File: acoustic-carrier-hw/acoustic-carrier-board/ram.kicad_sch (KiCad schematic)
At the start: 15 parts, among them IC1 ECP5-BGA256, IC2 MT41K256M16TW-107_P

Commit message: [carrier] Added separate buses for ddr3 ctrl-cmd and dq-groups
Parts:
- removed C40, C46: 0.1uF, Capacitor_SMD:C_0402_1005Metric, symbol Device:C_Small
- removed C47: 1uF, Capacitor_SMD:C_0805_2012Metric, symbol Device:C_Small
- removed C70: 22uF, Capacitor_SMD:C_0603_1608Metric, symbol Device:C_Small
- removed IC2: MT41K256M16TW-107_P, fpga:BGA96C80P9X16_800X1400X120, symbol MT41K256M16TW-107-P:MT41K256M16TW-107_P
- added C120, C58, C59: 10nF, Capacitor_SMD:C_0402_1005Metric, symbol Device:C_Small
- added C121, C122, C124, C125, C126, C49, C57: 0.1uF, Capacitor_SMD:C_0402_1005Metric, symbol Device:C_Small
- added C123, C127: 22uF, Capacitor_SMD:C_0603_1608Metric, symbol Device:C_Small
- added C5, C6: 10uF, Capacitor_SMD:C_0603_1608Metric, symbol Device:C_Small
- added IC3: MT41K256M16TW-107_P, fpga:BGA96C80P9X16_800X1400X120, symbol MT41K256M16TW-107-P:MT41K256M16TW-107_P
- added L10, L11, L9: 120@100MHz, Inductor_SMD:L_0603_1608Metric, symbol Device:L_Small
- C34, C35: value 22uF -> 10nF; footprint Capacitor_SMD:C_0603_1608Metric -> Capacitor_SMD:C_0402_1005Metric; LPN C59461 -> CL05B103KB5NNNC; MPN CL10A226MQ8NRNC -> C15195
- C37, C42: value 0.1uF -> 10nF; LPN C307331 -> CL05B103KB5NNNC; MPN CL05B104KB54PNC -> C15195
- C43: value 10nF -> 0.1uF; LPN CL05B103KB5NNNC -> C307331; MPN C15195 -> CL05B104KB54PNC
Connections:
- net GND: now also C120.2, C121.2, C122.2, C123.2, C124.2, C125.2, C126.2, C127.2, C49.2, C5.2, C57.2, C58.2, C59.2, C6.2, IC3.A9 (VSS_1), IC3.B1 (VSSQ_1), IC3.B3 (VSS_2), IC3.B9 (VSSQ_2), IC3.D1 (VSSQ_3), IC3.D8 (VSSQ_4), IC3.E1 (VSS_3), IC3.E2 (VSSQ_5), IC3.E8 (VSSQ_6), IC3.F9 (VSSQ_7), IC3.G1 (VSSQ_8), IC3.G8 (VSS_4), IC3.G9 (VSSQ_9), IC3.J2 (VSS_5), IC3.J8 (VSS_6), IC3.M1 (VSS_7), IC3.M9 (VSS_8), IC3.P1 (VSS_9), IC3.P9 (VSS_10), IC3.T1 (VSS_11), IC3.T9 (VSS_12)
- net VDDR3L_0.675: no longer IC1.G14 (PR14C/VREF1_2)
- net VDDR3L_1.35: now also L10.2, L11.2, L9.2; no longer C34.1, C35.1, C37.1, C42.1, IC1.H11 (VCCIO2_1), IC1.J11 (VCCIO2_2), IC1.J6 (VCCIO6_1), IC1.J7 (VCCIO6_2)
- net VDRR3L_0.675: now also IC1.G14 (PR14C/VREF1_2), C120.1, C121.1, IC3.H1 (VREFDQ), IC3.M8 (VREFCA); no longer C39.1, C43.1
- net LPDDR3.LDM: now reaches IC1.F13 (PR8C)
- net LPDDR3.LDM: now also IC3.E7 (LDM)
- net LPDDR3.DQ14: now reaches IC1.J15 (PR23B/PCLKC2_1)
- net LPDDR3.DQ14: now also IC3.B8 (DQ14)
- net LPDDR3.DQ13: now reaches IC1.J16 (PR23A/PCLKT2_1)
- net LPDDR3.DQ13: now also IC3.A2 (DQ13)
- net LPDDR3.DQ12: now reaches IC1.K14 (PR20D/GR_PCLK2_0)
- net LPDDR3.DQ12: now also IC3.A7 (DQ12)
- net LPDDR3.UDM: now reaches IC1.K15 (PR23D/PCLKC2_0/RDQ20)
- net LPDDR3.UDM: now also IC3.D3 (UDM)
- net LPDDR3.DQ15: now reaches IC1.K16 (PR23C/PCLKT2_0)
- net LPDDR3.DQ15: now also IC3.A3 (DQ15)
- net LPDDR3.A14: now reaches IC1.L1 (PL26A/LDQ32/PCLKT6_1)
- net LPDDR3.A14: now also IC3.T7 (A14)
- net at R54.1: now also IC3.L8 (ZQ)
- net RAM_A0 renamed LPDDR3.A0
- net LPDDR3.A0: now also IC3.N3 (A0)
- net RAM_A1 renamed LPDDR3.A1
- net LPDDR3.A1: now also IC3.P7 (A1)
- net RAM_A10 renamed LPDDR3.A9
- net LPDDR3.A9: now also IC3.R3 (A9)
- net RAM_A11 renamed LPDDR3.A10
- net LPDDR3.A10: now also IC3.L7 (A10/AP)
- net RAM_A12 renamed LPDDR3.A11
- net LPDDR3.A11: now also IC3.R7 (A11)
- net RAM_A13 renamed LPDDR3.A12
- net LPDDR3.A12: now also IC3.N7 (A12/BC#)
- net RAM_A14 renamed LPDDR3.A13
- net LPDDR3.A13: now also IC3.T3 (A13)
- net RAM_A2: no longer names the net of IC1.M4 (PL35C)
- net RAM_A3 renamed LPDDR3.A2
- net LPDDR3.A2: now also IC3.P3 (A2)
- net RAM_A4 renamed LPDDR3.A3
- net LPDDR3.A3: now also IC3.N2 (A3)
- net RAM_A5 renamed LPDDR3.A4
- net LPDDR3.A4: now also IC3.P8 (A4)
- net RAM_A6 renamed LPDDR3.A5
- net LPDDR3.A5: now also IC3.P2 (A5)
- net RAM_A7 renamed LPDDR3.A6
- net LPDDR3.A6: now also IC3.R8 (A6)
- net RAM_A8 renamed LPDDR3.A7
- net LPDDR3.A7: now also IC3.R2 (A7)
- net RAM_A9 renamed LPDDR3.A8
- net LPDDR3.A8: now also IC3.T8 (A8)
- net RAM_BA0 renamed LPDDR3.ODT
- net LPDDR3.ODT: now also IC3.K1 (ODT)
- net RAM_BA1: no longer names the net of IC1.T2 (PL38D)
- net RAM_BA2: no longer names the net of IC1.R2 (PL38C)
- net RAM_CAS# renamed LPDDR3.BA2
- net LPDDR3.BA2: now also IC3.M3 (BA2)
- net RAM_CK+ renamed LPDDR3.CK#
- net LPDDR3.CK#: now also IC3.K7 (CK#)
- net RAM_CK- renamed LPDDR3.CK
- net LPDDR3.CK: now also IC3.J7 (CK)
- net RAM_CKE renamed LPDDR3.RAS#
- net LPDDR3.RAS#: now also IC3.J3 (RAS#)
- net RAM_CS# renamed LPDDR3.CKE
- net LPDDR3.CKE: now also IC3.K9 (CKE)
- net RAM_D0 renamed LPDDR3.DQ0
- net LPDDR3.DQ0: now also IC3.E3 (DQ0)
- net RAM_D1 renamed LPDDR3.DQ1
- net LPDDR3.DQ1: now also IC3.F7 (DQ1)
- net RAM_D10: no longer names the net of IC1.H14 (PR14D)
- net RAM_D11: no longer names the net of IC1.H12 (PR17A)
- net RAM_D12 renamed LPDDR3.DQ8
- net LPDDR3.DQ8: now also IC3.D7 (DQ8)
- net RAM_D13 renamed LPDDR3.DQ9
- net LPDDR3.DQ9: now also IC3.C3 (DQ9)
- net RAM_D14 renamed LPDDR3.DQ10
- net LPDDR3.DQ10: now also IC3.C8 (DQ10)
- net RAM_D15 renamed LPDDR3.DQ11
- net LPDDR3.DQ11: now also IC3.C2 (DQ11)
- net RAM_D2 renamed LPDDR3.DQ2
- net LPDDR3.DQ2: now also IC3.F2 (DQ2)
- net RAM_D3 renamed LPDDR3.DQ3
- net LPDDR3.DQ3: now also IC3.F8 (DQ3)
- net RAM_D4 renamed LPDDR3.DQ4
- net LPDDR3.DQ4: now also IC3.H3 (DQ4)
- net RAM_D5 renamed LPDDR3.DQ5
- net LPDDR3.DQ5: now also IC3.H8 (DQ5)
- net RAM_D6 renamed LPDDR3.DQ6
- net LPDDR3.DQ6: now also IC3.G2 (DQ6)
- net RAM_D7 renamed LPDDR3.DQ7
- net LPDDR3.DQ7: now also IC3.H7 (DQ7)
- net RAM_D8: no longer names the net of IC1.F16 (PR14A/RDQ20)
- net RAM_D9: no longer names the net of IC1.G15 (PR14B)
- net RAM_LDM renamed LPDDR3.CAS#
- net LPDDR3.CAS#: now also IC3.K3 (CAS#)
- net RAM_LDQS+ renamed LPDDR3.LDQS
- net LPDDR3.LDQS: now also IC3.F3 (LDQS)
- net RAM_LDQS- renamed LPDDR3.LDQS#
- net LPDDR3.LDQS#: now also IC3.G3 (LDQS#)
- net RAM_ODT renamed LPDDR3.BA0
- net LPDDR3.BA0: now also IC3.M2 (BA0)
- net RAM_RAS# renamed LPDDR3.BA1
- net LPDDR3.BA1: now also IC3.N8 (BA1)
- net RAM_RESET# renamed LPDDR3.WE#
- net LPDDR3.WE#: now also IC3.L3 (WE#)
- net RAM_UDM renamed LPDDR3.CS#
- net LPDDR3.CS#: now also IC3.L2 (CS#)
- net RAM_UDQS+ renamed LPDDR3.UDQS
- net LPDDR3.UDQS: now also IC3.B7 (UDQS#)
- net RAM_UDQS- renamed LPDDR3.UDQS#
- net LPDDR3.UDQS#: now also IC3.C7 (UDQS)
- net RAM_WE# renamed LPDDR3.RESET#
- net LPDDR3.RESET#: now also IC3.T2 (RESET#)
- new net VDDR_BANK: C49.1, C5.1, C57.1, C58.1, C59.1, C6.1, IC1.H11 (VCCIO2_1), IC1.J11 (VCCIO2_2), IC1.J6 (VCCIO6_1), IC1.J7 (VCCIO6_2), L11.1
- new net VDDR_CORE: C124.1, C125.1, C126.1, C127.1, C37.1, C42.1, IC3.B2 (VDD_1), IC3.D9 (VDD_2), IC3.G7 (VDD_3), IC3.K2 (VDD_4), IC3.K8 (VDD_5), IC3.N1 (VDD_6), IC3.N9 (VDD_7), IC3.R1 (VDD_8), IC3.R9 (VDD_9), L9.1
- new net VDDR_DQ: C122.1, C123.1, C34.1, C35.1, C39.1, C43.1, IC3.A1 (VDDQ_1), IC3.A8 (VDDQ_2), IC3.C1 (VDDQ_3), IC3.C9 (VDDQ_4), IC3.D2 (VDDQ_5), IC3.E9 (VDDQ_6), IC3.F1 (VDDQ_7), IC3.H2 (VDDQ_8), IC3.H9 (VDDQ_9), L10.1
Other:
- note added: "DDR3L DECOUPLING"
- moved on the sheet: C38, C80, IC1D, IC1F, R54

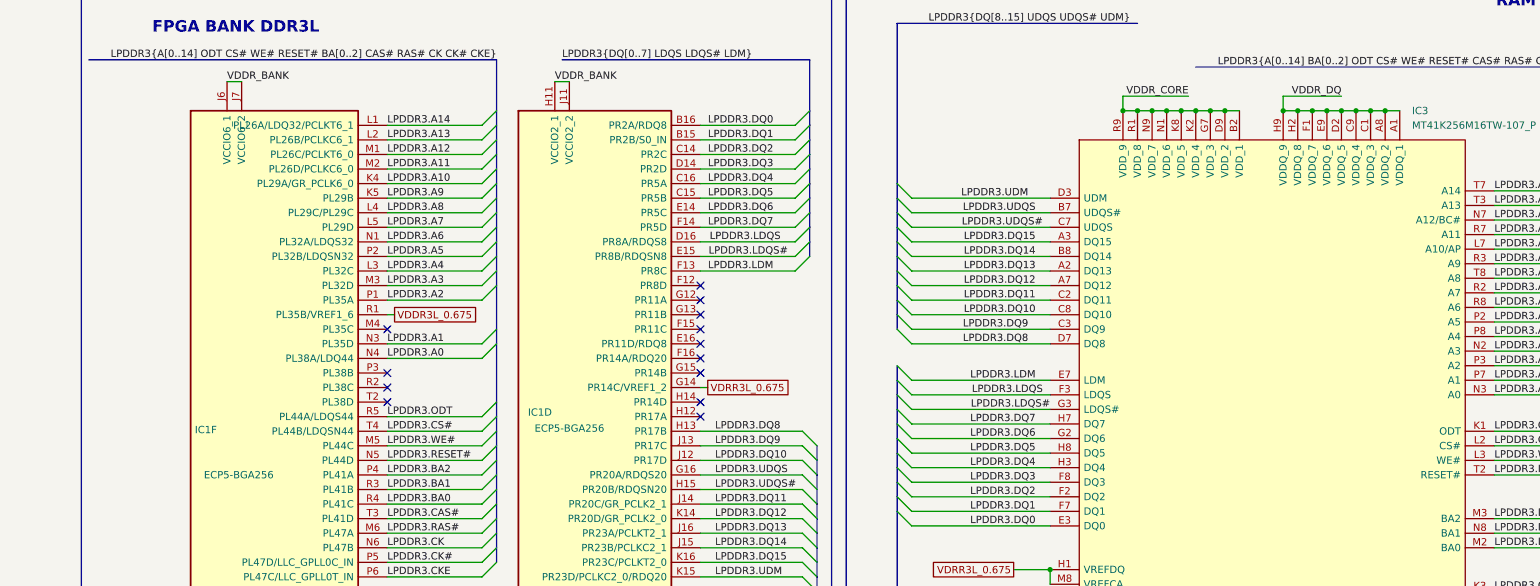
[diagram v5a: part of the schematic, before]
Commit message: [carrier] Fixed error in ethernet power supply, separated footprints + symbols into library (next) check whether supply should be DVDDH
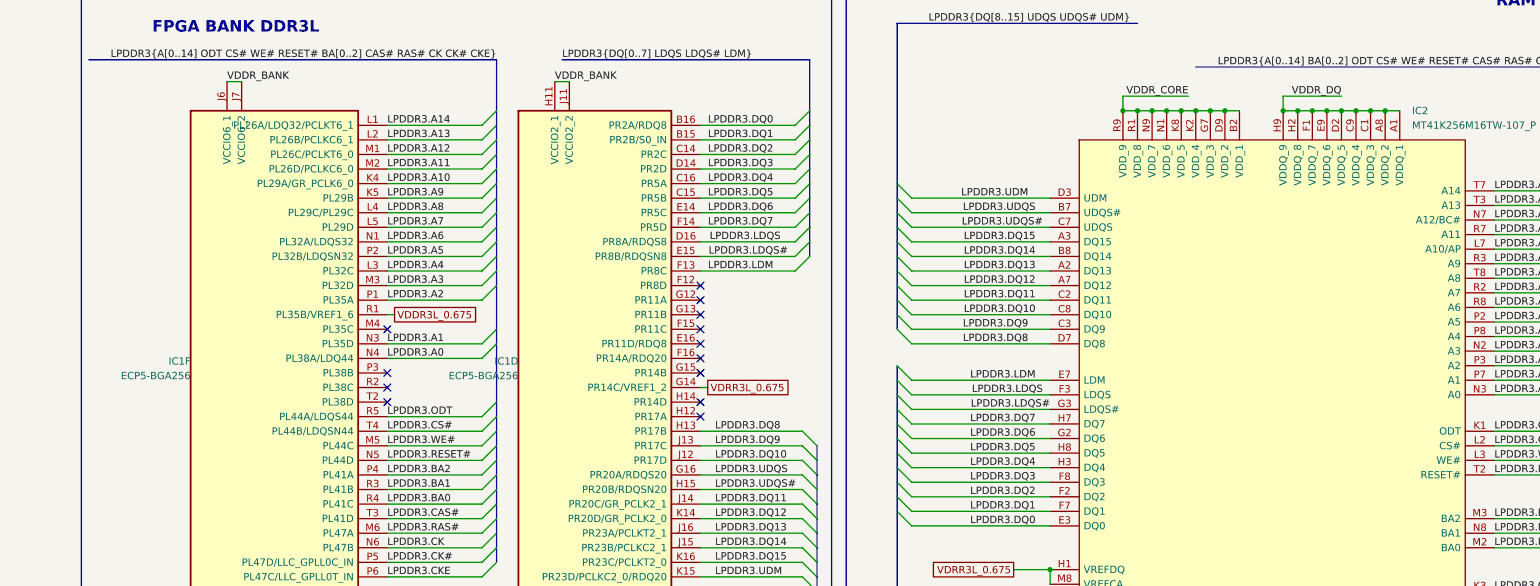
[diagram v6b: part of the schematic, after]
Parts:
- removed IC1: ECP5-BGA256, fpga:BGA256C80P16X16_1400X1400X170, symbol ecp5bga256:ECP5-BGA256
- removed IC3: MT41K256M16TW-107_P, fpga:BGA96C80P9X16_800X1400X120, symbol MT41K256M16TW-107-P:MT41K256M16TW-107_P
- added IC1: ECP5-BGA256, iw-fpga_mcu:BGA256C80P16X16_1400X1400X170, symbol iw-fpga_mcu:ECP5-BGA256
- added IC2: MT41K256M16TW-107_P, iw-memory:BGA96C80P9X16_800X1400X120, symbol iw-memory:MT41K256M16TW-107_P
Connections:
- net GND: now also IC2.A9 (VSS_1), IC2.B1 (VSSQ_1), IC2.B3 (VSS_2), IC2.B9 (VSSQ_2), IC2.D1 (VSSQ_3), IC2.D8 (VSSQ_4), IC2.E1 (VSS_3), IC2.E2 (VSSQ_5), IC2.E8 (VSSQ_6), IC2.F9 (VSSQ_7), IC2.G1 (VSSQ_8), IC2.G8 (VSS_4), IC2.G9 (VSSQ_9), IC2.J2 (VSS_5), IC2.J8 (VSS_6), IC2.M1 (VSS_7), IC2.M9 (VSS_8), IC2.P1 (VSS_9), IC2.P9 (VSS_10), IC2.T1 (VSS_11), IC2.T9 (VSS_12)
- net LPDDR3.A0: now also IC1.N4 (PL38A/LDQ44), IC2.N3 (A0)
- net LPDDR3.A1: now also IC1.N3 (PL35D), IC2.P7 (A1)
- net LPDDR3.A10: now also IC1.K4 (PL29A/GR_PCLK6_0), IC2.L7 (A10/AP)
- net LPDDR3.A11: now also IC1.M2 (PL26D/PCLKC6_0), IC2.R7 (A11)
- net LPDDR3.A12: now also IC1.M1 (PL26C/PCLKT6_0), IC2.N7 (A12/BC#)
- net LPDDR3.A13: now also IC1.L2 (PL26B/PCLKC6_1), IC2.T3 (A13)
- net LPDDR3.A14: now also IC1.L1 (PL26A/LDQ32/PCLKT6_1), IC2.T7 (A14)
- net LPDDR3.A2: now also IC1.P1 (PL35A), IC2.P3 (A2)
- net LPDDR3.A3: now also IC1.M3 (PL32D), IC2.N2 (A3)
- net LPDDR3.A4: now also IC1.L3 (PL32C), IC2.P8 (A4)
- net LPDDR3.A5: now also IC1.P2 (PL32B/LDQSN32), IC2.P2 (A5)
- net LPDDR3.A6: now also IC1.N1 (PL32A/LDQS32), IC2.R8 (A6)
- net LPDDR3.A7: now also IC1.L5 (PL29D), IC2.R2 (A7)
- net LPDDR3.A8: now also IC1.L4 (PL29C/PL29C), IC2.T8 (A8)
- net LPDDR3.A9: now also IC1.K5 (PL29B), IC2.R3 (A9)
- net LPDDR3.BA0: now also IC1.R4 (PL41C), IC2.M2 (BA0)
- net LPDDR3.BA1: now also IC1.R3 (PL41B), IC2.N8 (BA1)
- net LPDDR3.BA2: now also IC1.P4 (PL41A), IC2.M3 (BA2)
- net LPDDR3.CAS#: now also IC1.T3 (PL41D), IC2.K3 (CAS#)
- net LPDDR3.CK: now also IC1.N6 (PL47B), IC2.J7 (CK)
- net LPDDR3.CK#: now also IC1.P5 (PL47D/LLC_GPLL0C_IN), IC2.K7 (CK#)
- net LPDDR3.CKE: now also IC1.P6 (PL47C/LLC_GPLL0T_IN), IC2.K9 (CKE)
- net LPDDR3.CS#: now also IC1.T4 (PL44B/LDQSN44), IC2.L2 (CS#)
- net LPDDR3.DQ0: now also IC1.B16 (PR2A/RDQ8), IC2.E3 (DQ0)
- net LPDDR3.DQ1: now also IC1.B15 (PR2B/S0_IN), IC2.F7 (DQ1)
- net LPDDR3.DQ10: now also IC1.J12 (PR17D), IC2.C8 (DQ10)
- net LPDDR3.DQ11: now also IC1.J14 (PR20C/GR_PCLK2_1), IC2.C2 (DQ11)
- net LPDDR3.DQ12: now also IC1.K14 (PR20D/GR_PCLK2_0), IC2.A7 (DQ12)
- net LPDDR3.DQ13: now also IC1.J16 (PR23A/PCLKT2_1), IC2.A2 (DQ13)
- net LPDDR3.DQ14: now also IC1.J15 (PR23B/PCLKC2_1), IC2.B8 (DQ14)
- net LPDDR3.DQ15: now also IC1.K16 (PR23C/PCLKT2_0), IC2.A3 (DQ15)
- net LPDDR3.DQ2: now also IC1.C14 (PR2C), IC2.F2 (DQ2)
- net LPDDR3.DQ3: now also IC1.D14 (PR2D), IC2.F8 (DQ3)
- net LPDDR3.DQ4: now also IC1.C16 (PR5A), IC2.H3 (DQ4)
- net LPDDR3.DQ5: now also IC1.C15 (PR5B), IC2.H8 (DQ5)
- net LPDDR3.DQ6: now also IC1.E14 (PR5C), IC2.G2 (DQ6)
- net LPDDR3.DQ7: now also IC1.F14 (PR5D), IC2.H7 (DQ7)
- net LPDDR3.DQ8: now also IC1.H13 (PR17B), IC2.D7 (DQ8)
- net LPDDR3.DQ9: now also IC1.J13 (PR17C), IC2.C3 (DQ9)
- net LPDDR3.LDM: now also IC1.F13 (PR8C), IC2.E7 (LDM)
- net LPDDR3.LDQS: now also IC1.D16 (PR8A/RDQS8), IC2.F3 (LDQS)
- net LPDDR3.LDQS#: now also IC1.E15 (PR8B/RDQSN8), IC2.G3 (LDQS#)
- net LPDDR3.ODT: now also IC1.R5 (PL44A/LDQS44), IC2.K1 (ODT)
- net LPDDR3.RAS#: now also IC1.M6 (PL47A), IC2.J3 (RAS#)
- net LPDDR3.RESET#: now also IC1.N5 (PL44D), IC2.T2 (RESET#)
- net LPDDR3.UDM: now also IC1.K15 (PR23D/PCLKC2_0/RDQ20), IC2.D3 (UDM)
- net LPDDR3.UDQS: now also IC1.G16 (PR20A/RDQS20), IC2.B7 (UDQS#)
- net LPDDR3.UDQS#: now also IC1.H15 (PR20B/RDQSN20), IC2.C7 (UDQS)
- net LPDDR3.WE#: now also IC1.M5 (PL44C), IC2.L3 (WE#)
- net VDDR3L_0.675: now also IC1.R1 (PL35B/VREF1_6)
- net VDDR_BANK: now also IC1.H11 (VCCIO2_1), IC1.J11 (VCCIO2_2), IC1.J6 (VCCIO6_1), IC1.J7 (VCCIO6_2)
- net VDDR_CORE: now also IC2.B2 (VDD_1), IC2.D9 (VDD_2), IC2.G7 (VDD_3), IC2.K2 (VDD_4), IC2.K8 (VDD_5), IC2.N1 (VDD_6), IC2.N9 (VDD_7), IC2.R1 (VDD_8), IC2.R9 (VDD_9)
- net VDDR_DQ: now also IC2.A1 (VDDQ_1), IC2.A8 (VDDQ_2), IC2.C1 (VDDQ_3), IC2.C9 (VDDQ_4), IC2.D2 (VDDQ_5), IC2.E9 (VDDQ_6), IC2.F1 (VDDQ_7), IC2.H2 (VDDQ_8), IC2.H9 (VDDQ_9)
- net VDRR3L_0.675: now also IC1.G14 (PR14C/VREF1_2), IC2.H1 (VREFDQ), IC2.M8 (VREFCA)
- net at R54.1: now also IC2.L8 (ZQ)

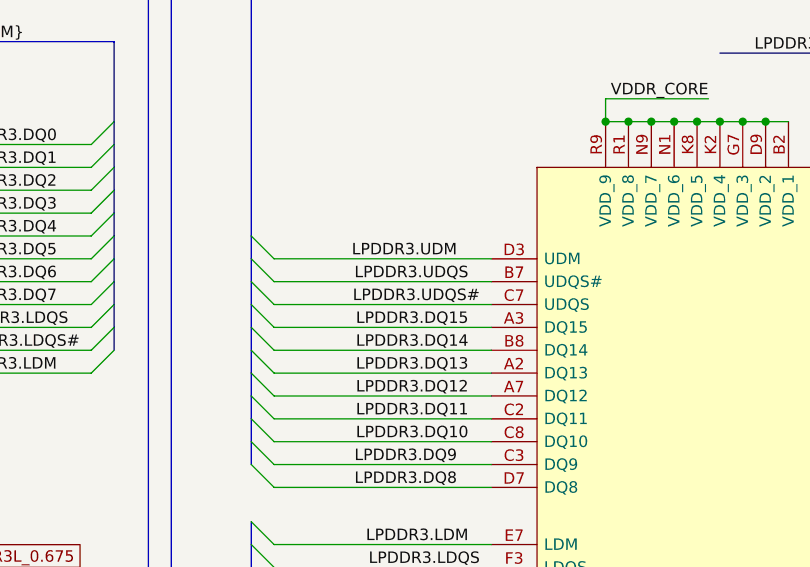
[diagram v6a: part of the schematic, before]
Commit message: [carrier] Signal switch-around in ddr3
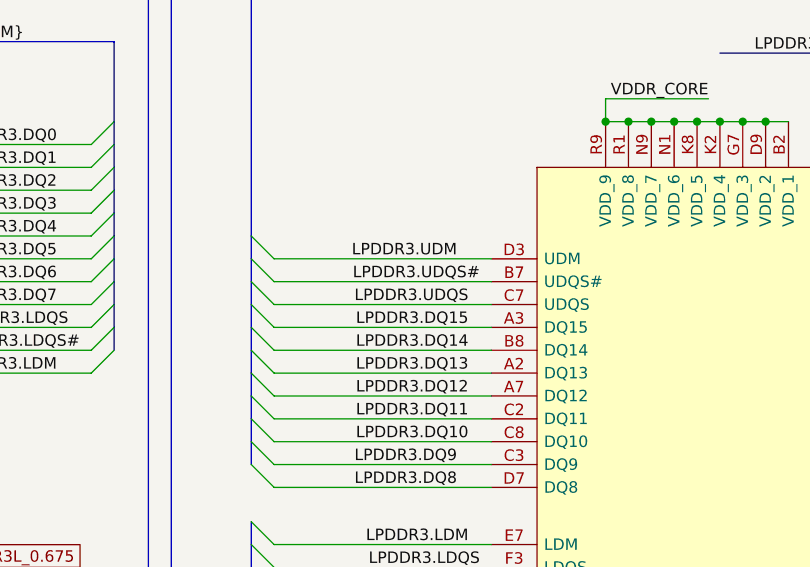
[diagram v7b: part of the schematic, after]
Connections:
- net LPDDR3.UDQS: now also IC2.C7 (UDQS); no longer IC2.B7 (UDQS#)
- net LPDDR3.UDQS#: now also IC2.B7 (UDQS#); no longer IC2.C7 (UDQS)
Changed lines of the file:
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@@
 		)
 	)
-	(label "LPDDR3.UDQS"
-		(at 181.61 53.34 180)
+	(label "LPDDR3.UDQS#"
+		(at 182.88 53.34 180)
 		(effects
 			(font
@@
 		)
 	)
-	(label "LPDDR3.UDQS#"
-		(at 182.88 55.88 180)
+	(label "LPDDR3.UDQS"
+		(at 181.61 55.88 180)
 		(effects
 			(font
